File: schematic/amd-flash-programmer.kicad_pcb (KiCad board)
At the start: 2 copper layers, 60 x 90 mm, 15 parts, among them U1 AM29F040B-90PC, U2 74HC595, U3 74HC595

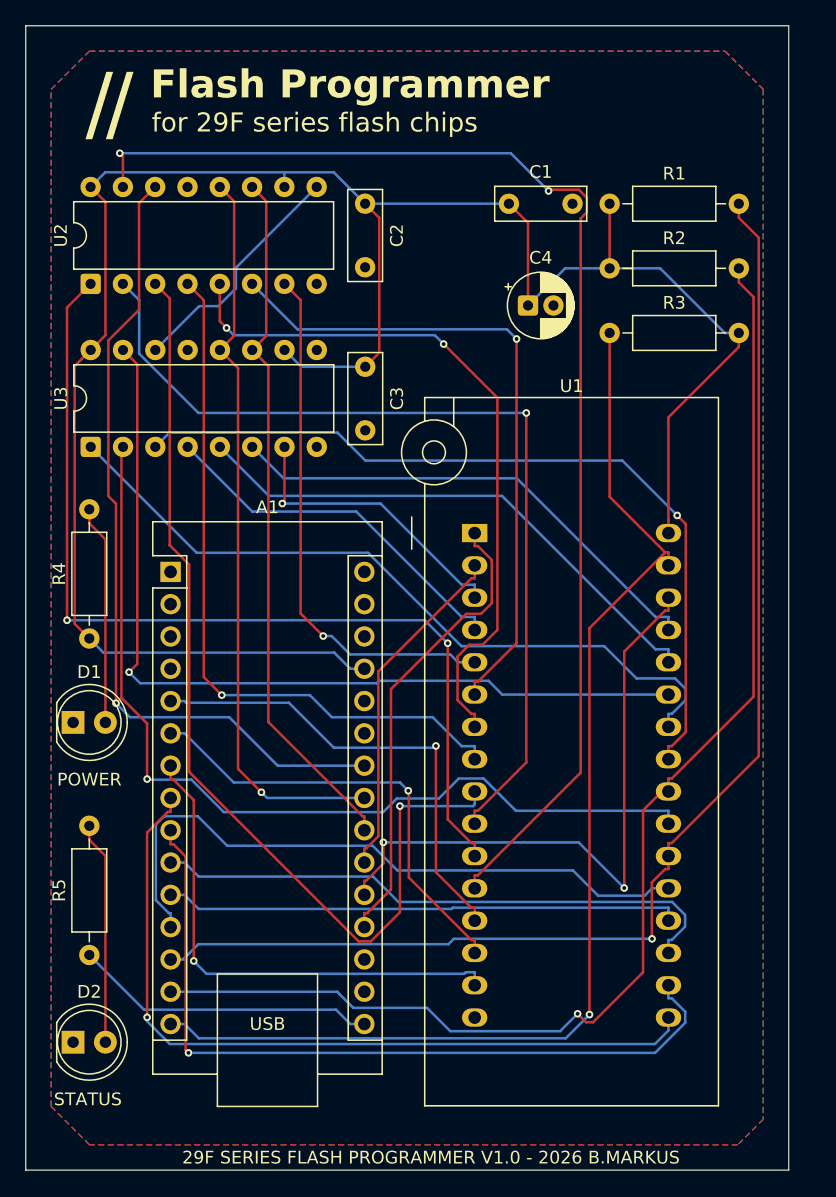
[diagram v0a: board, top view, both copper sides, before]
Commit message: PCB rerouted without vias, silkscreen updated
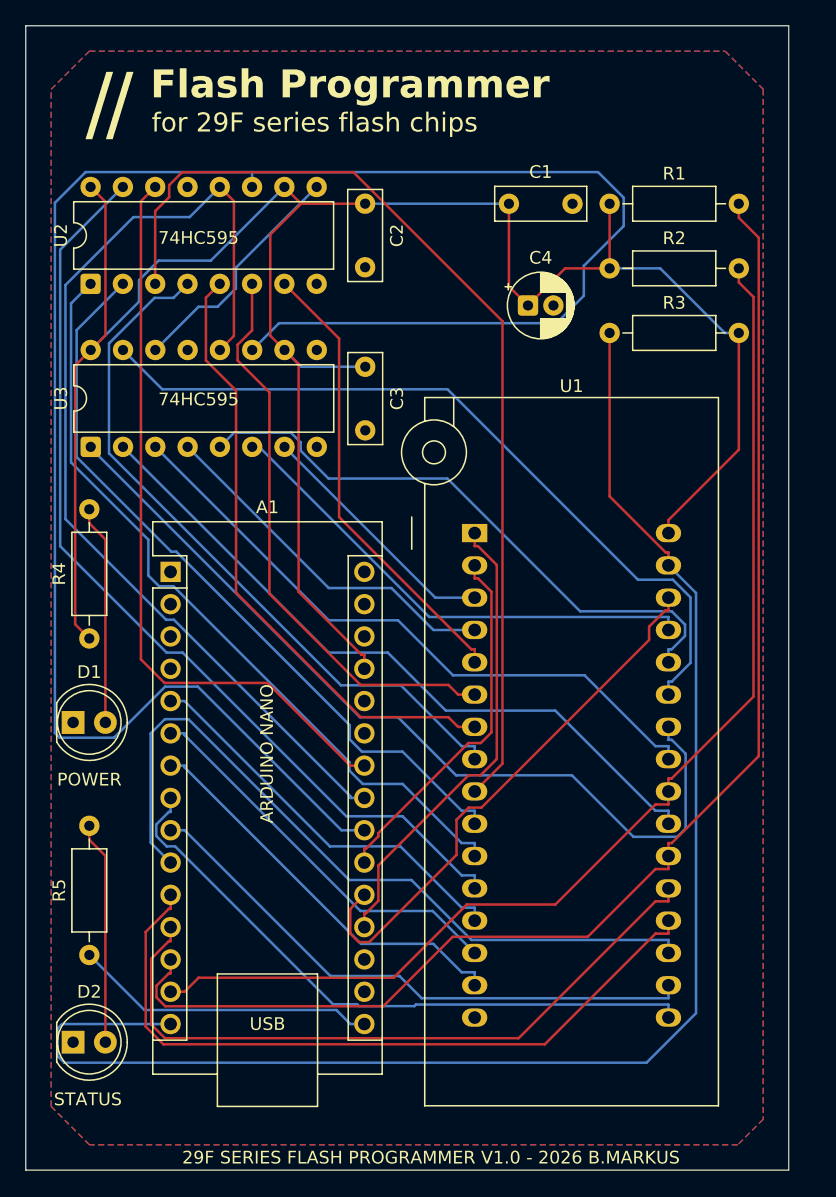
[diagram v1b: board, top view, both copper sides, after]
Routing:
- net Net-(A1-A3): track 55.2 -> 157.1 mm
- net Net-(A1-D12): track 93.3 -> 119.7 mm, vias 1 -> 0
- net /A0: track 99.1 -> 74.6 mm, vias 2 -> 0
- net Net-(A1-A4): track 58.2 -> 80.1 mm, vias 1 -> 0
- net /D6: track 40.7 -> 57.6 mm
- net /A10: track 72.3 -> 55.8 mm, vias 1 -> 0
- net /D4: track 61.9 -> 45.7 mm, vias 1 -> 0
- net /D5: track 45.9 -> 60.2 mm
- net /A1: track 75.7 -> 61.9 mm, vias 2 -> 0
- net /A11: track 64.4 -> 51.1 mm, vias 1 -> 0
- net /A2: track 72.5 -> 59.6 mm, vias 1 -> 0
- net /D3: track 61.7 -> 50.4 mm, vias 1 -> 0
- net Net-(A1-D11): track 101.0 -> 90.8 mm, vias 1 -> 0
- net /A9: track 58.4 -> 68.5 mm
- net +5V: track 167.9 -> 176.5 mm
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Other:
- board text added: "74HC595"
- board text added: "ARDUINO NANO"

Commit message: PCB updated
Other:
- board text added: "29F SERIES FLASH PROGRAMMER V1.0 - 2026 B. MARKUS"
- board text removed: "29F SERIES FLASH PROGRAMMER V1.0 - 2026 B.MARKUS"
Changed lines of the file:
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@@
 		)
 	)
-	(gr_text "29F SERIES FLASH PROGRAMMER V1.0 - 2026 B.MARKUS"
-		(at 12.3 89.6 0)
+	(gr_text "29F SERIES FLASH PROGRAMMER V1.0 - 2026 B. MARKUS"
+		(at 11.176 89.6 0)
 		(layer "F.SilkS")
 		(effects
